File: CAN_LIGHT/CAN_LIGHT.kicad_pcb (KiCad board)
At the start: 2 copper layers, 135.5 x 115.4 mm, 190 parts, among them J1 Conn_ARM_SWD_TagConnect_TC2030, J2 436500428, J3 430450428, J4 Conn_ARM_SWD_TagConnect_TC203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, U1 MSPM0C1103SDDFR, U5 XMSM0G3507SDGS28R

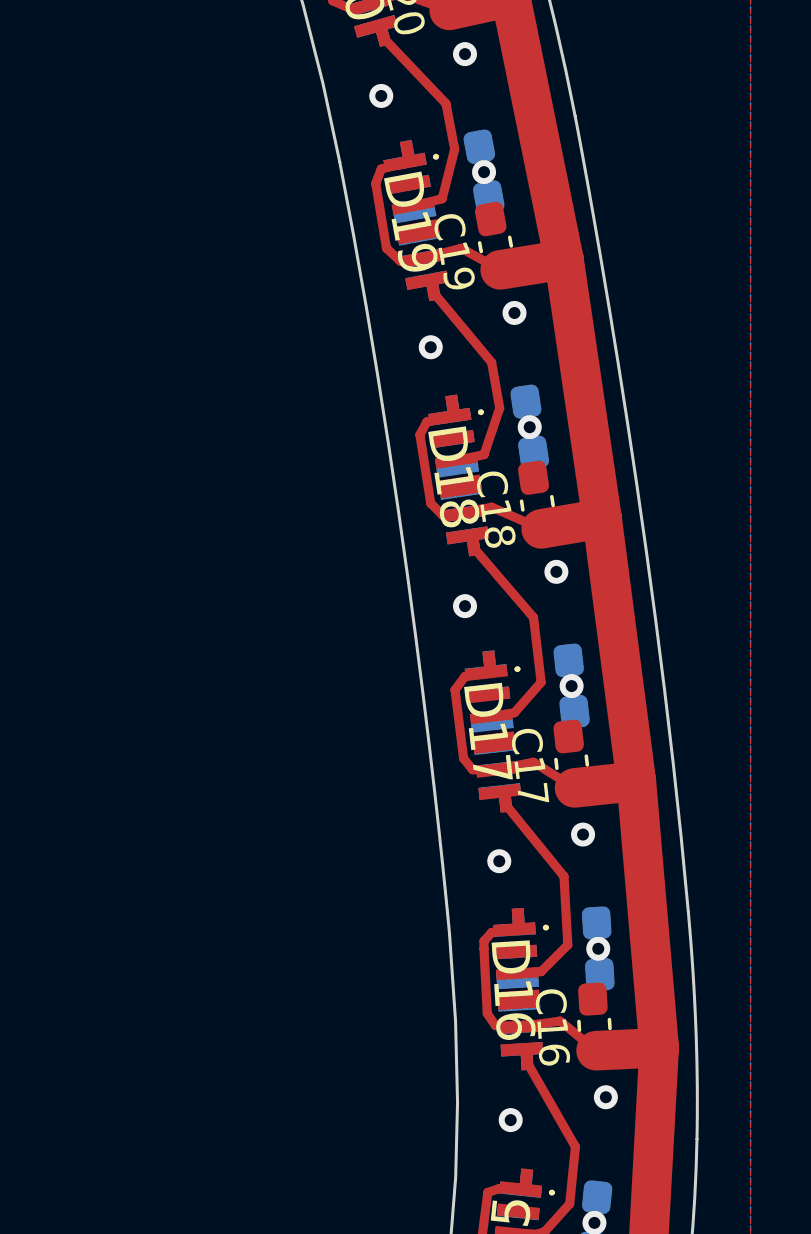
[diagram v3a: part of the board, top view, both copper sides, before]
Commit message: Route some more bottom level 5V
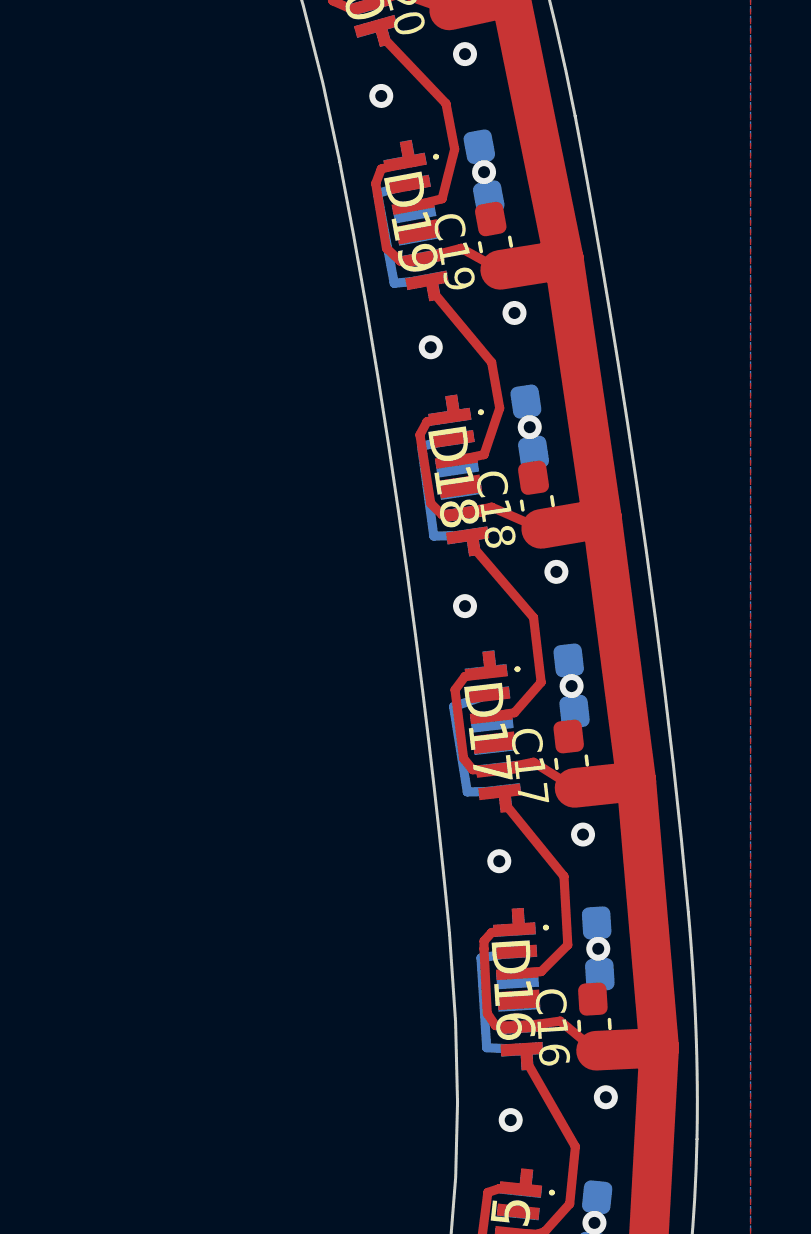
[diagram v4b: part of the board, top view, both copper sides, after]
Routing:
- net +5V: track 870.1 -> 891.1 mm
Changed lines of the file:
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@@
   (segment (start 69.696524 91.226265) (end 67.564 91.567) (width 1.3208) (layer "F.Cu") (net 3))
   (segment (start 144.78 127.508) (end 144.314684 128.527978) (width 0.3048) (layer "B.Cu") (net 3))
+  (segment (start 193.278943 91.962787) (end 192.2272 92.202) (width 0.3048) (layer "B.Cu") (net 3))
   (segment (start 139.446 125.8316) (end 136.7028 124.9172) (width 0.3048) (layer "B.Cu") (net 3))
+  (segment (start 190.754 83.7692) (end 191.815057 83.468885) (width 0.3048) (layer "B.Cu") (net 3))
   (segment (start 120.1928 119.5832) (end 119.727484 120.603178) (width 0.3048) (layer "B.Cu") (net 3))
   (segment (start 82.671917 107.856221) (end 82.9056 106.934) (width 0.3048) (layer "B.Cu") (net 3))
@@
   (segment (start 188.0616 132.588) (end 185.674 134.2136) (width 0.3048) (layer "B.Cu") (net 3))
   (segment (start 139.221316 126.884188) (end 139.446 125.8316) (width 0.3048) (layer "B.Cu") (net 3))
+  (segment (start 193.7512 103.7336) (end 193.294 100.8888) (width 0.3048) (layer "B.Cu") (net 3))
   (segment (start 180.6448 135.8392) (end 177.6476 136.144) (width 0.3048) (layer "B.Cu") (net 3))
+  (segment (start 195.373117 109.077722) (end 194.2084 109.2708) (width 0.3048) (layer "B.Cu") (net 3))
   (segment (start 147.405618 129.532283) (end 147.6248 128.4224) (width 0.3048) (layer "B.Cu") (net 3))
   (segment (start 95.668182 112.849683) (end 96.105408 111.955008) (width 0.25) (layer "B.Cu") (net 3))
@@
   (segment (start 172.18908 136.837422) (end 172.2628 135.6868) (width 0.3048) (layer "B.Cu") (net 3))
   (segment (start 188.788985 133.421945) (end 188.0616 132.588) (width 0.3048) (layer "B.Cu") (net 3))
+  (segment (start 193.294 100.8888) (end 194.468811 100.487794) (width 0.3048) (layer "B.Cu") (net 3))
   (segment (start 103.9368 114.2492) (end 103.344484 115.319978) (width 0.3048) (layer "B.Cu") (net 3))
   (segment (start 163.788618 134.815483) (end 164.0332 133.7564) (width 0.3048) (layer "B.Cu") (net 3))
+  (segment (start 192.407323 86.664463) (end 191.3128 86.7664) (width 0.3048) (layer "B.Cu") (net 3))
   (segment (start 114.639618 118.940483) (end 114.8588 117.9068) (width 0.3048) (layer "B.Cu") (net 3))
   (segment (start 90.7796 110.1852) (end 88.138 109.22) (width 0.3048) (layer "B.Cu") (net 3))
@@
   (segment (start 164.0332 133.7564) (end 161.0868 132.7912) (width 0.3048) (layer "B.Cu") (net 3))
   (segment (start 87.898393 109.335993) (end 88.138 109.22) (width 0.3048) (layer "B.Cu") (net 3))
+  (segment (start 192.6336 95.1992) (end 192.2272 92.202) (width 0.3048) (layer "B.Cu") (net 3))
   (segment (start 161.0868 132.7912) (end 160.697684 133.811178) (width 0.3048) (layer "B.Cu") (net 3))
   (segment (start 112.1156 116.8908) (end 111.548684 117.936178) (width 0.3048) (layer "B.Cu") (net 3))
@@
   (segment (start 106.7308 115.1128) (end 103.9368 114.2492) (width 0.3048) (layer "B.Cu") (net 3))
   (segment (start 90.568428 111.206016) (end 90.7796 110.1852) (width 0.3048) (layer "B.Cu") (net 3))
+  (segment (start 191.3128 86.7664) (end 190.754 83.7692) (width 0.3048) (layer "B.Cu") (net 3))
+  (segment (start 195.571525 112.32166) (end 194.398698 112.268) (width 0.3048) (layer "B.Cu") (net 3))
+  (segment (start 193.759324 95.177089) (end 192.6336 95.1992) (width 0.3048) (layer "B.Cu") (net 3))
   (segment (start 79.701949 106.386606) (end 80.3656 105.5116) (width 0.3048) (layer "B.Cu") (net 3))
   (segment (start 155.8544 131.064) (end 152.9588 130.1496) (width 0.3048) (layer "B.Cu") (net 3))
@@
   (segment (start 82.9056 106.934) (end 81.28 106.0196) (width 0.3048) (layer "B.Cu") (net 3))
   (segment (start 82.516532 108.011606) (end 82.671917 107.856221) (width 0.3048) (layer "B.Cu") (net 3))
+  (segment (start 194.836721 103.716903) (end 193.7512 103.7336) (width 0.3048) (layer "B.Cu") (net 3))
   (segment (start 80.3656 105.5116) (end 81.28 106.0196) (width 0.3048) (layer "B.Cu") (net 3))
   (segment (start 169.3164 135.1788) (end 168.988455 136.273065) (width 0.3048) (layer "B.Cu") (net 3))
   (segment (start 177.6476 136.144) (end 177.635262 137.263161) (width 0.3048) (layer "B.Cu") (net 3))
+  (segment (start 194.2084 109.2708) (end 194.398698 112.268) (width 0.3048) (layer "B.Cu") (net 3))
   (segment (start 90.297 112.8268) (end 89.685416 111.863584) (width 0.254) (layer "F.Cu") (net 8))
   (segment (start 90.297 112.8268) (end 92.329 113.538) (width 0.254) (layer "F.Cu") (net 8))

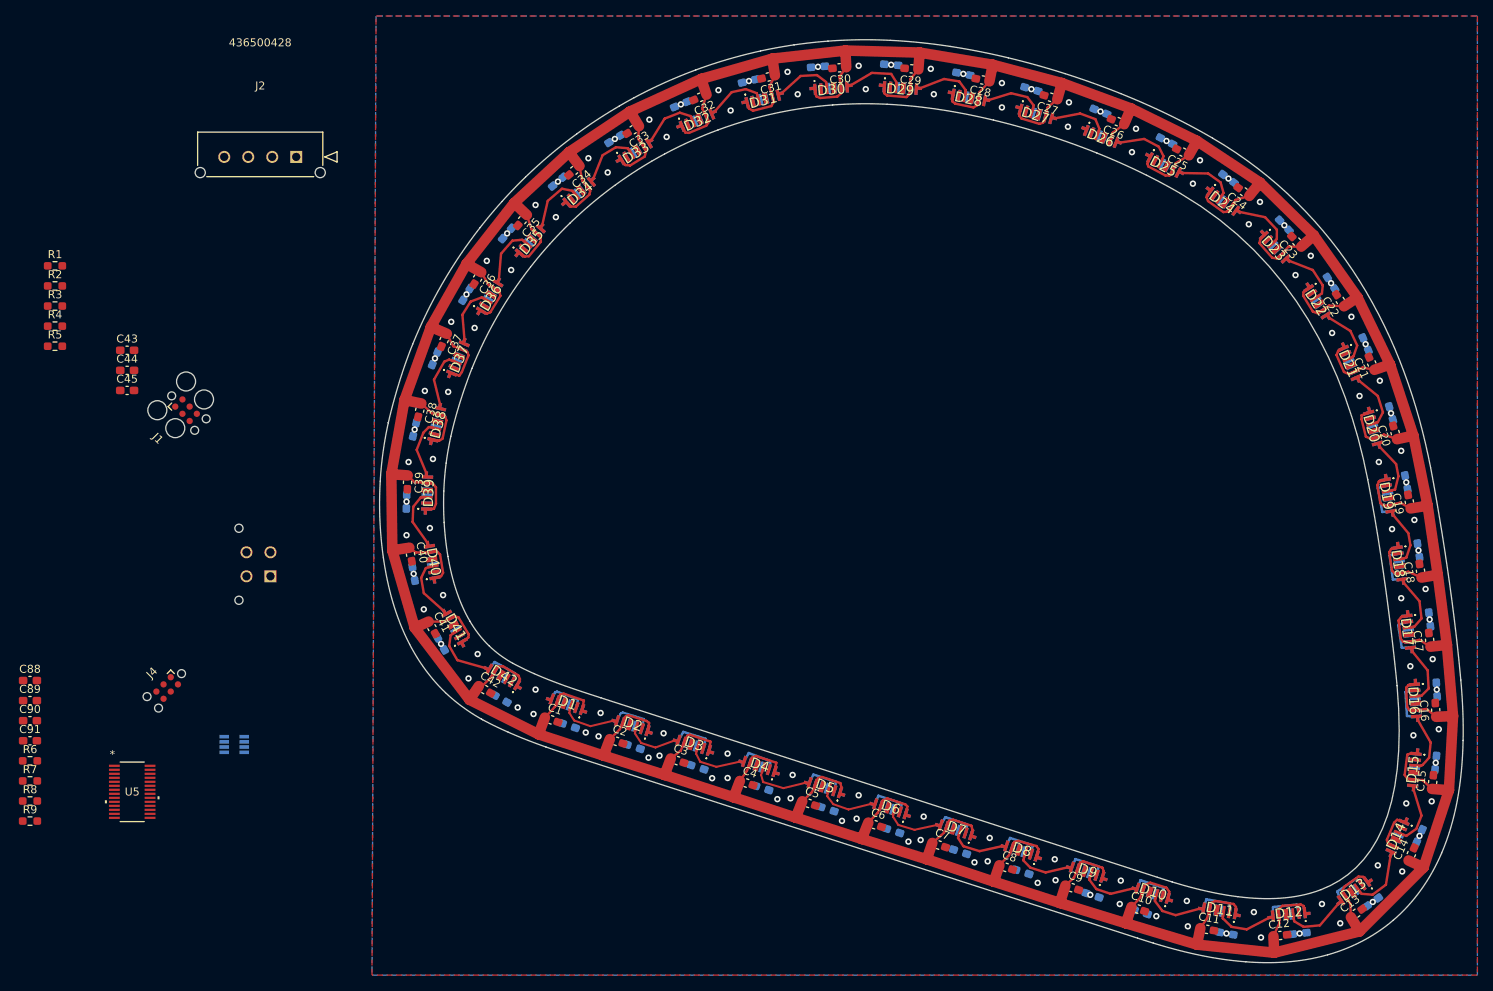
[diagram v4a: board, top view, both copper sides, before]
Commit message: Route bottom level 5V LED traces and GND vias
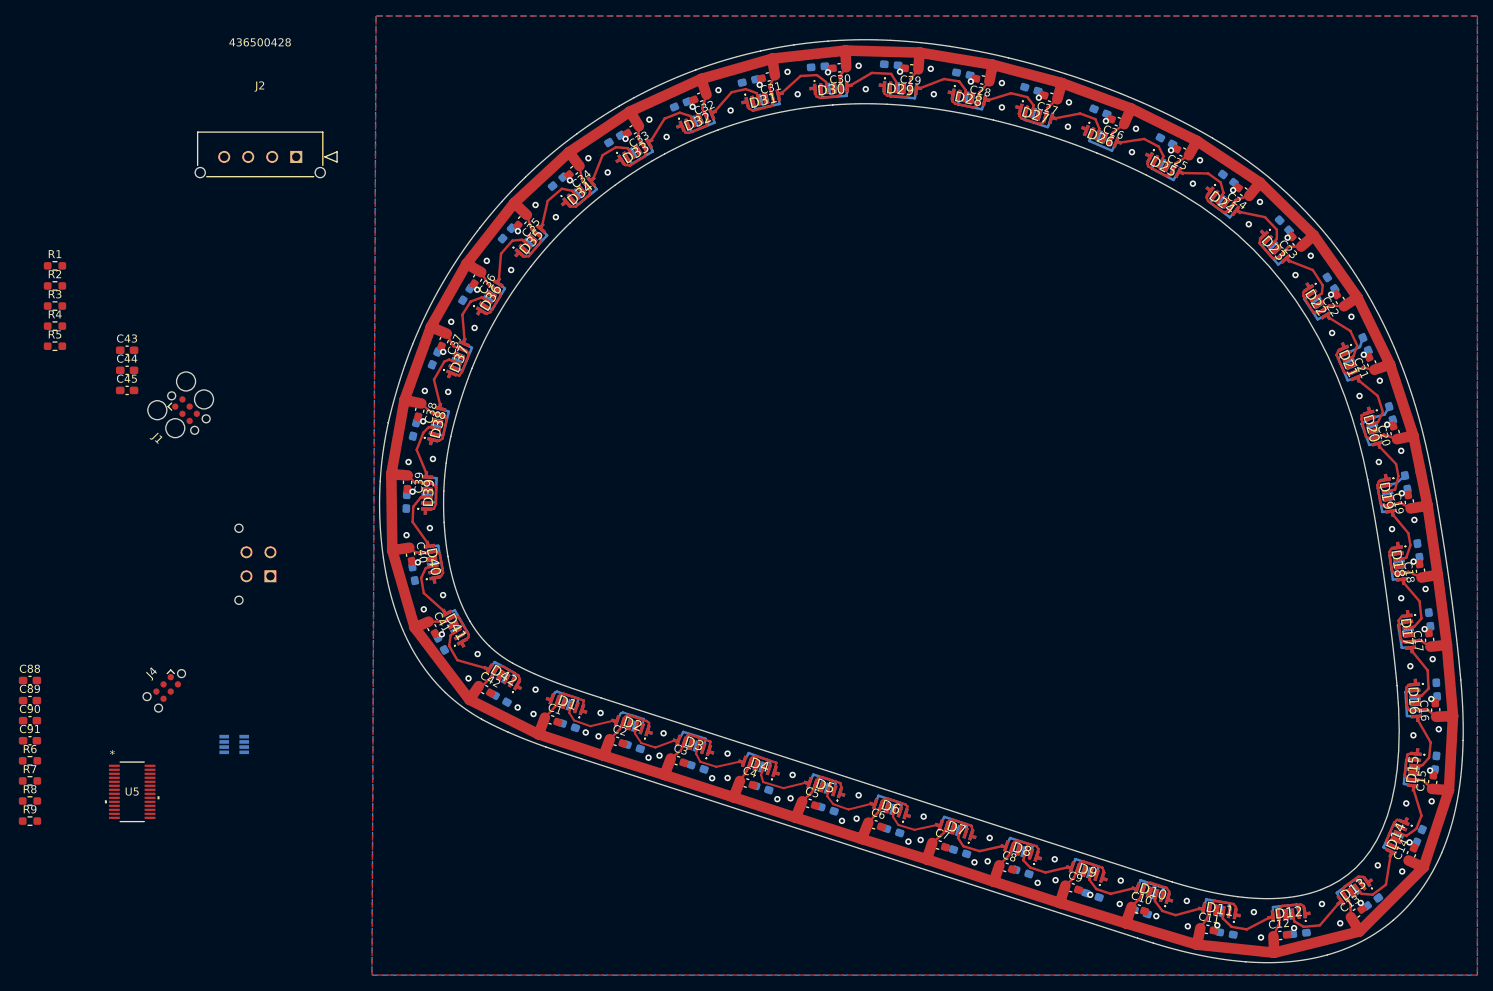
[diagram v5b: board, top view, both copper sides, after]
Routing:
- net +5V: track 891.1 -> 1027.2 mm

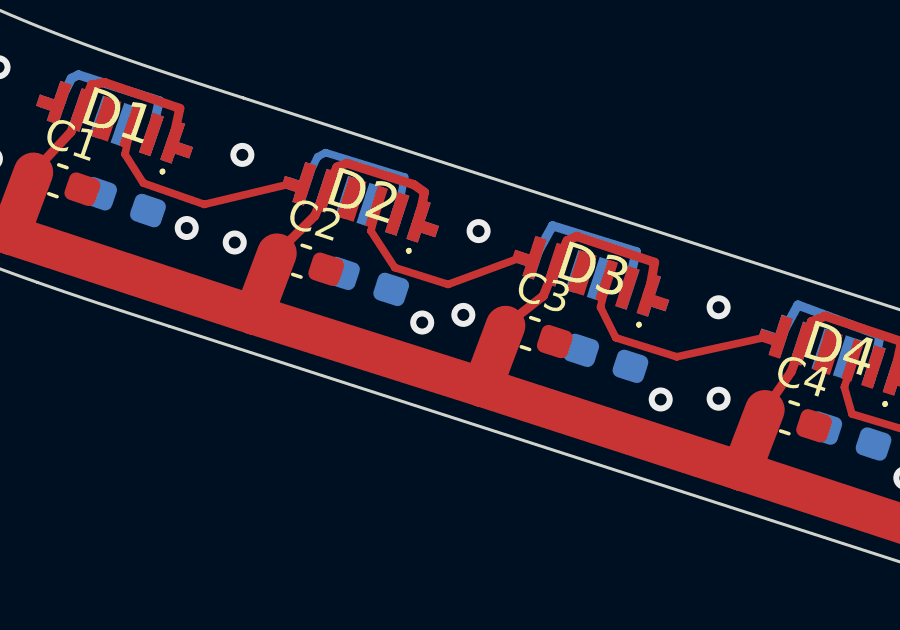
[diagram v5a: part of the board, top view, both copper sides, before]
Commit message: Route bottom 5V to larger rail
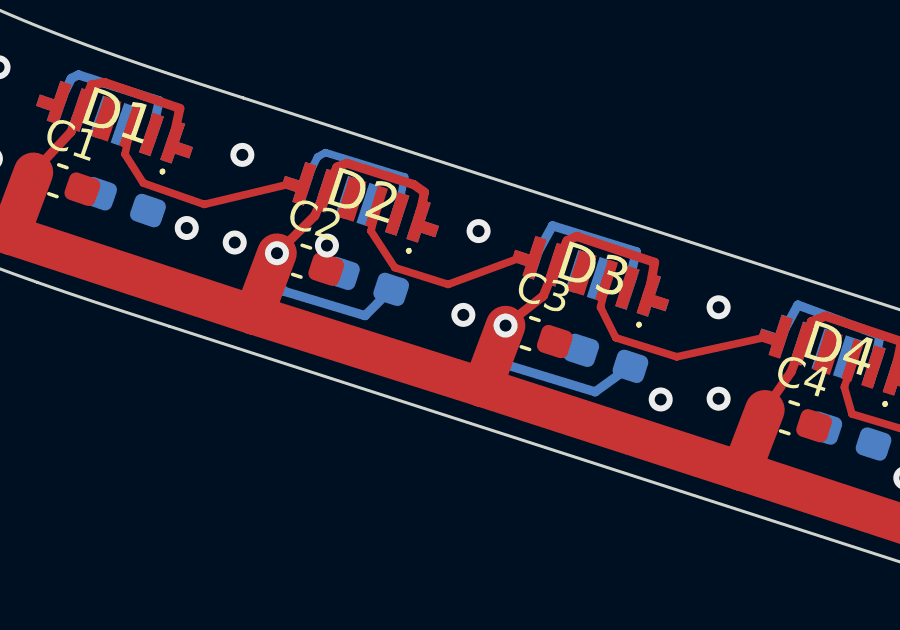
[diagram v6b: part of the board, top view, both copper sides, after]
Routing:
- net +5V: track 1027.2 -> 1038.6 mm, vias 0 -> 2
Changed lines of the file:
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@@
   (via (at 180.2892 138.7856) (size 0.8) (drill 0.4) (layers "F.Cu" "B.Cu") (free) (net 2))
   (via (at 185.039 64.389) (size 0.8) (drill 0.4) (layers "F.Cu" "B.Cu") (free) (net 2))
-  (via (at 99.5934 117.475) (size 0.8) (drill 0.4) (layers "F.Cu" "B.Cu") (free) (net 2))
+  (via (at 96.4184 114.9096) (size 0.8) (drill 0.4) (layers "F.Cu" "B.Cu") (free) (net 2))
   (via (at 99.695 37.719) (size 0.8) (drill 0.4) (layers "F.Cu" "B.Cu") (free) (net 2))
   (via (at 78.232 104.521) (size 0.8) (drill 0.4) (layers "F.Cu" "B.Cu") (free) (net 2))
@@
   (segment (start 118.813714 122.923473) (end 117.983 124.968) (width 1.3208) (layer "F.Cu") (net 3))
   (segment (start 69.696524 91.226265) (end 67.564 91.567) (width 1.3208) (layer "F.Cu") (net 3))
+  (via (at 94.752428 115.163946) (size 0.8) (drill 0.4) (layers "F.Cu" "B.Cu") (net 3))
+  (via (at 102.372428 117.576946) (size 0.8) (drill 0.4) (layers "F.Cu" "B.Cu") (net 3))
   (segment (start 73.1012 82.55) (end 72.9996 85.5472) (width 0.3048) (layer "B.Cu") (net 3))
   (segment (start 136.5504 124.8664) (end 139.446 125.8316) (width 0.3048) (layer "B.Cu") (net 3))
@@
   (segment (start 157.5308 41.6052) (end 154.686 40.386) (width 0.3048) (layer "B.Cu") (net 3))
   (segment (start 80.782869 58.18502) (end 81.6356 58.8264) (width 0.3048) (layer "B.Cu") (net 3))
+  (segment (start 94.584185 115.8748) (end 94.752428 115.163946) (width 0.3048) (layer "B.Cu") (net 3))
   (segment (start 86.9188 52.1716) (end 84.836 54.5084) (width 0.3048) (layer "B.Cu") (net 3))
   (segment (start 136.130382 125.879883) (end 136.5504 124.8664) (width 0.3048) (layer "B.Cu") (net 3))
@@
   (segment (start 81.6356 58.8264) (end 80.0608 61.468) (width 0.3048) (layer "B.Cu") (net 3))
   (segment (start 141.598475 35.327461) (end 141.2748 36.4236) (width 0.3048) (layer "B.Cu") (net 3))
+  (segment (start 97.6884 117.2464) (end 94.996 116.434406) (width 0.3048) (layer "B.Cu") (net 3))
   (segment (start 195.373117 109.077722) (end 194.2084 109.2708) (width 0.3048) (layer "B.Cu") (net 3))
   (segment (start 191.815057 83.468885) (end 193.0908 83.1596) (width 0.3048) (layer "B.Cu") (net 3))
+  (segment (start 102.362 118.872) (end 102.372428 117.576946) (width 0.3048) (layer "B.Cu") (net 3))
   (segment (start 149.5044 38.6588) (end 146.6088 37.7444) (width 0.3048) (layer "B.Cu") (net 3))
   (segment (start 105.0036 39.2684) (end 104.483415 38.266578) (width 0.3048) (layer "B.Cu") (net 3))
@@
   (segment (start 115.9764 35.7632) (end 112.9792 36.4236) (width 0.3048) (layer "B.Cu") (net 3))
   (segment (start 192.409236 129.213239) (end 191.4652 128.6764) (width 0.3048) (layer "B.Cu") (net 3))
+  (segment (start 105.3592 119.7864) (end 102.362 118.872) (width 0.3048) (layer "B.Cu") (net 3))
   (segment (start 112.9792 36.4236) (end 112.656849 35.428733) (width 0.3048) (layer "B.Cu") (net 3))
+  (segment (start 106.535086 118.935327) (end 105.3592 119.7864) (width 0.3048) (layer "B.Cu") (net 3))
   (segment (start 76.9112 101.7016) (end 75.950478 102.305744) (width 0.3048) (layer "B.Cu") (net 3))
+  (segment (start 94.584185 115.8748) (end 94.996 116.434406) (width 0.3048) (layer "B.Cu") (net 3))
   (segment (start 121.3104 34.9504) (end 124.3584 34.7472) (width 0.3048) (layer "B.Cu") (net 3))
   (segment (start 193.0908 83.1596) (end 194.152822 82.209943) (width 0.3048) (layer "B.Cu") (net 3))
@@
   (segment (start 107.8484 38.1) (end 105.0036 39.2684) (width 0.3048) (layer "B.Cu") (net 3))
   (segment (start 131.2672 123.19) (end 128.3208 122.2248) (width 0.3048) (layer "B.Cu") (net 3))
+  (segment (start 98.559486 116.369927) (end 97.6884 117.2464) (width 0.3048) (layer "B.Cu") (net 3))
   (segment (start 106.7308 115.1128) (end 103.9368 114.2492) (width 0.3048) (layer "B.Cu") (net 3))
   (segment (start 172.998879 49.111075) (end 172.2628 49.9364) (width 0.3048) (layer "B.Cu") (net 3))
